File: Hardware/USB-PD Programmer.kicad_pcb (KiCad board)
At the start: 2 copper layers, 34 x 34 mm, 24 parts, among them J1 Conn_01x08_Male, J2 Conn_01x04_Male, J3 Conn_01x02_Male, J4 Conn_01x02_Male, J5 Conn_01x02_Male, J6 Conn_01x02_Male, J7 Conn_01x07_Male, U1 R1501J033B-T1-JE, U2 CH340G, Y1 12M

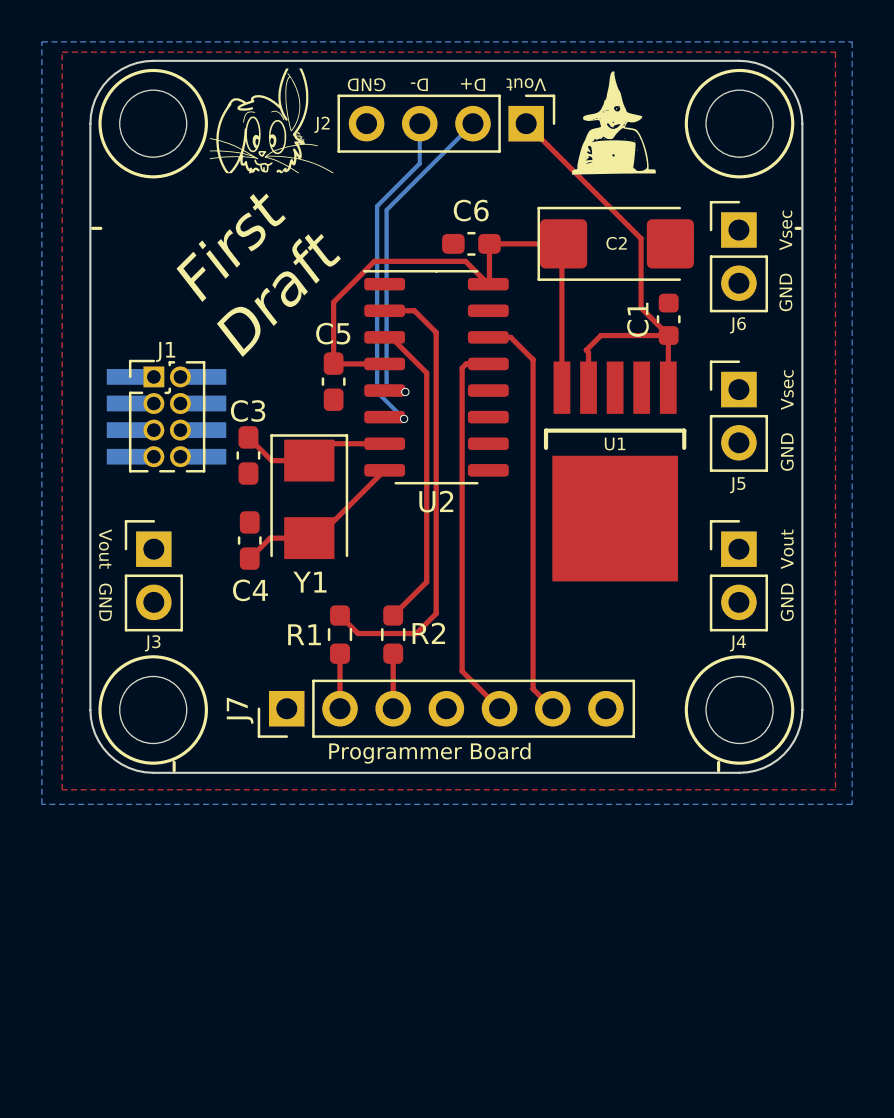
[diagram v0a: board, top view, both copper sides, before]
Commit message: Cleaned up design of the Programmer board
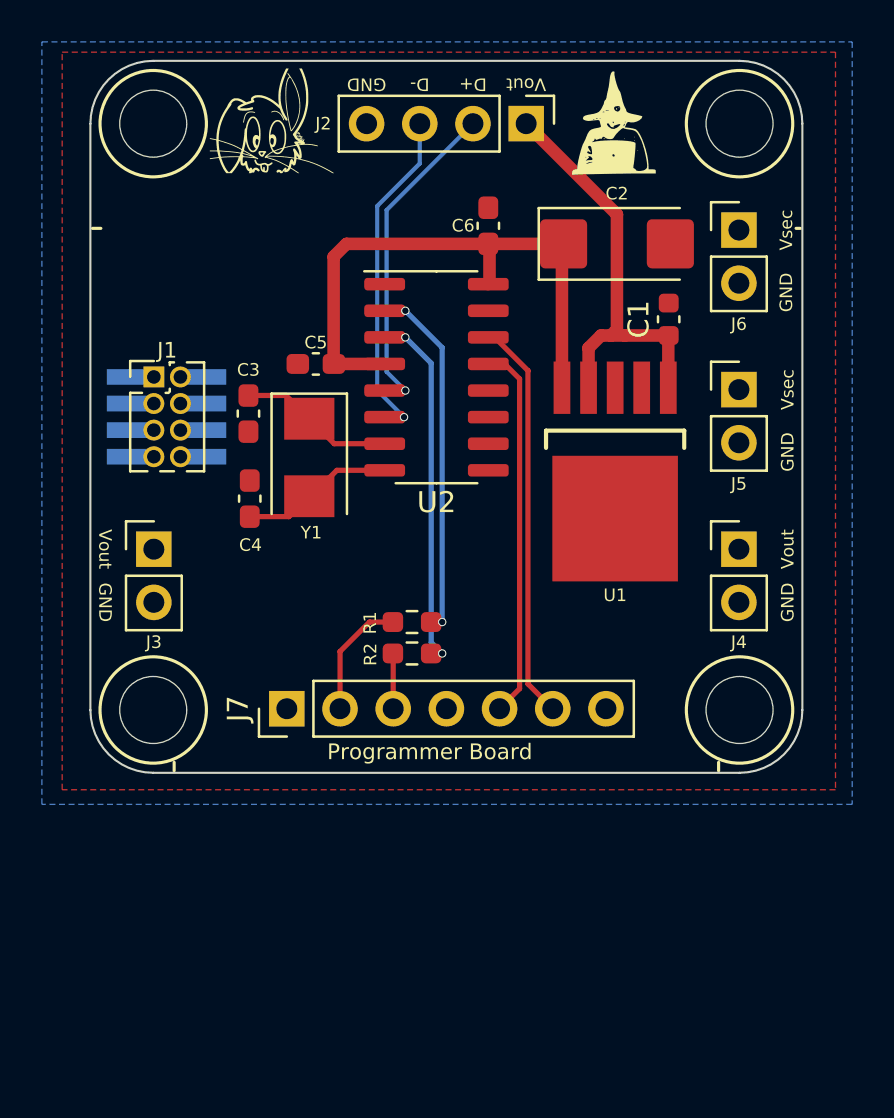
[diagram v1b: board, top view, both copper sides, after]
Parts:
- C3, C4: value 22p -> 20p
- moved R1 3.49 mm to (98.4, 96.8), turned to 180 degrees
- moved C3 2.00 mm to (90.5, 86.8)
- moved C4 2.00 mm to (90.6, 90.9)
- moved Y1 2.00 mm to (93.5, 88.9)
- moved R2 1.27 mm to (98.4, 98.3), turned to 180 degrees
- moved C5 1.20 mm to (93.8, 84.5), turned to 180 degrees
- moved C6 1.18 mm to (102.0, 77.9), turned to 90 degrees
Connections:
- net RxD renamed IO3
- net TxD renamed IO1
- net Vcc2 renamed Vsec
- J7 pad 4: unconnected-(J7-Pad4) -> GND
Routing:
- net Net-(R1-Pad1): track 21.7 -> 15.6 mm, vias 0 -> 2
- net IO3: track 2.53 -> 5.84 mm
- net Vsec: track 26.4 -> 27.6 mm
- net Vout: track 21.5 -> 20.5 mm
- net Net-(R2-Pad1): track 15.0 -> 15.8 mm, vias 0 -> 2
- net /XO: track 8.19 -> 7.36 mm
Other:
- board text removed: "First Draft"

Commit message: Documentation...
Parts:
- added JP1: SolderJumper_2_Open, Tinker:SolderJumper-2_P_Open_Rounded_skinny, F.Cu at (93.3, 78.7)
- U2: value CH340G -> CH340G/C
- moved G*** 17.6 mm to (90.4, 72.9)
- moved REF** 16.6 mm to (108.0, 73.5)
- renumbered J7 to J1, J1 to J7
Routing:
- net +3V3: track 0.00 -> 22.4 mm, vias 0 -> 1
- net Vsec: track 27.6 -> 28.6 mm
- net DTR: track 17.9 -> 17.1 mm, vias 0 -> 1
- net RTS: track 19.2 -> 19.4 mm, vias 0 -> 1
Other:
- board text added: "3v3"
- board text added: "DTR"
- board text added: "RST"
- board text added: "RTS"
- board text added: "RxD"
- board text added: "TxD"

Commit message: Tinkerin' + RESET & LED on Programmer...
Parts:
- added D2: XL-2012RGBC, Tinker:XL-2012RGBC, F.Cu at (96.2, 97.4)
- added R4: 10K, Resistor_SMD:R_0603_1608Metric_Pad0.98x0.95mm_HandSolder, F.Cu at (100.0, 97.4)
- added SW1: SW_Push, Tinker:SW_Push_TS273014TP, F.Cu at (105.8, 96.5)
- moved R1 5.32 mm to (98.4, 91.5)
- moved R2 5.32 mm to (98.4, 93.0)
- moved C1 1.94 mm to (108.9, 81.4), turned to 0 degrees
- moved U1 0.60 mm to (108.1, 89.1)
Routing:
- net +3V3: track 22.4 -> 51.0 mm
- net RST: track 0.00 -> 7.27 mm
- net IO1: track 2.53 -> 8.59 mm
- net Net-(R2-Pad1): track 15.8 -> 10.5 mm
- net Net-(R1-Pad1): track 15.6 -> 10.3 mm
- net IO3: track 5.84 -> 10.6 mm
- net Net-(D2-Pad3): track 0.00 -> 2.86 mm
- net GND: track 0.00 -> 2.63 mm, vias 0 -> 9
- net Vout: track 20.5 -> 19.3 mm
- net Vsec: track 28.6 -> 28.0 mm
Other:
- board text added: "${TITLE}"
- board text added: "NerdMage Modules ${TITLE} (v${REVISION})"
- board text added: "R - TxD G - Rxd"
- board text added: "RESET"
- board text removed: "NerdMage Modules (v0.0.1)"
- board text removed: "Programmer Board"

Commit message: Programmer Board Indicators!
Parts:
- removed D2: XL-2012RGBC, Tinker:XL-2012RGBC
- removed R4: 10K, Resistor_SMD:R_0603_1608Metric_Pad0.98x0.95mm_HandSolder
- added D4: red, LED_SMD:LED_0603_1608Metric, F.Cu at (97.5, 97.6)
- added D5: green, LED_SMD:LED_0603_1608Metric, F.Cu at (94.9, 97.6)
- added D6: yellow, LED_SMD:LED_0603_1608Metric, F.Cu at (102.5, 97.6)
- added D7: yellow, LED_SMD:LED_0603_1608Metric, F.Cu at (105.1, 97.6)
- added R6: 1k, Resistor_SMD:R_0603_1608Metric, F.Cu at (97.5, 94.6)
- added R7: 1k, Resistor_SMD:R_0603_1608Metric, F.Cu at (94.9, 94.6)
- added R8: 1k, Resistor_SMD:R_0603_1608Metric, F.Cu at (102.5, 94.6)
- added R9: 1k, Resistor_SMD:R_0603_1608Metric, F.Cu at (105.1, 94.6)
- moved SW1 14.4 mm to (91.4, 95.8), turned to 90 degrees
- moved C4 1.90 mm to (91.2, 89.1)
- moved R1 1.80 mm to (98.4, 89.7)
- moved R2 1.80 mm to (98.4, 91.2)
- moved Y1 1.55 mm to (93.9, 87.4)
- moved C5 1.54 mm to (94.1, 83.0)
- moved C1 1.50 mm to (108.9, 79.9)
- moved C2 1.50 mm to (108.1, 77.2)
- moved C6 1.50 mm to (102.0, 76.4)
- moved U1 1.50 mm to (108.1, 87.6)
- moved U2 1.50 mm to (99.5, 83.6)
- moved C3 1.32 mm to (91.2, 85.7)
- moved JP1 1.12 mm to (93.6, 79.8)
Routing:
- net +3V3: track 51.0 -> 28.2 mm
- net RST: track 7.27 -> 25.9 mm
- net Vsec: track 28.0 -> 40.3 mm
- net DTR: track 17.1 -> 21.1 mm
- net RTS: track 19.4 -> 23.5 mm
- net Net-(D2-Pad3): track 2.86 -> 0.00 mm
- net GND: track 2.63 -> 0.00 mm
- net IO3: track 10.6 -> 12.7 mm
- net IO1: track 8.59 -> 10.4 mm
- net UD-: track 15.4 -> 13.9 mm
- net UD+: track 14.8 -> 13.3 mm
- net Net-(R8-Pad1): track 0.00 -> 1.39 mm
- net Net-(R7-Pad2): track 0.00 -> 1.39 mm
- net Net-(R6-Pad2): track 0.00 -> 1.39 mm
- net Net-(D7-Pad2): track 0.00 -> 1.39 mm
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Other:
- board text removed: "R - TxD G - Rxd"

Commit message: possibly, maybe, finalised Programmer Board?
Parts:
- moved SW1 17.9 mm to (109.3, 96.2), turned to -90 degrees
- moved R2 0.60 mm to (98.4, 91.8)
- moved U1 0.50 mm to (108.1, 87.1)
- moved R1 0.30 mm to (98.4, 90.0)
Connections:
- SW1 pad 2: +3V3 -> Vsec
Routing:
- net RST: track 25.9 -> 7.64 mm
- net +3V3: track 28.2 -> 21.2 mm
- net Vsec: track 40.3 -> 47.3 mm
- net Vout: track 19.0 -> 18.1 mm
- net Net-(R2-Pad1): track 10.2 -> 10.8 mm
- net IO1: track 10.4 -> 9.78 mm
- net GND: vias 9 -> 0

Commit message: Rabbit OCD attack...
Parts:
- added D1: blue, LED_SMD:LED_0603_1608Metric, F.Cu at (92.4, 97.6)
- added R1: 1k, Resistor_SMD:R_0603_1608Metric, F.Cu at (92.4, 94.6)
- renumbered D4 to D2, D5 to D3, D6 to D4, D7 to D5, R6 to R2, R7 to R3, R8 to R4, R9 to R5, R1 to R6, R2 to R7
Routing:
- net +3V3: track 21.2 -> 23.7 mm
- net Net-(D1-Pad1): track 0.00 -> 1.39 mm
- net DTR: track 21.1 -> 22.0 mm

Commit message: Uber Rework!
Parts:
- J1: footprint Connector_PinHeader_2.54mm:PinHeader_1x07_P2.54mm_Vertical -> Tinker:Board_Stacker_7
- J2: footprint Tinker:PinHeader_1x04_P2.54mm_Vertical -> Tinker:Board_Stacker_4
- J3, J4, J5, J6: footprint Tinker:PinHeader_1x02_P2.54mm_Vertical -> Tinker:Board_Stacker_2
- moved J1 13.6 mm to (96.2, 114.0)
- moved C6 13.3 mm to (102.0, 89.7)
- moved G*** 13.3 mm to (93.0, 85.9)
- moved SW1 13.2 mm to (107.8, 109.3), turned to 180 degrees
- moved J2 13.1 mm to (101.9, 86.0)
- moved D1 13.0 mm to (94.9, 110.4)
- moved R1 13.0 mm to (94.9, 107.4)
- moved REF** 13.0 mm to (107.0, 86.5)
- moved J3 13.0 mm to (86.0, 106.3)
- moved J5 13.0 mm to (114.0, 98.7)
- moved J6 13.0 mm to (114.0, 91.1)
- moved J7 13.0 mm to (86.0, 98.1)
- moved C1 13.0 mm to (108.9, 92.9)
- moved C2 13.0 mm to (108.1, 90.2)
- moved C3 13.0 mm to (91.2, 98.7)
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- renumbered D3 to D2, D2 to D3, R3 to R2, R2 to R3
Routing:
- net +3V3: track 23.7 -> 26.2 mm
- net Vout: track 18.1 -> 20.0 mm
- net DTR: track 22.0 -> 20.8 mm
- net Vsec: track 47.3 -> 46.4 mm
- net RST: track 7.64 -> 8.44 mm
- net RTS: track 23.5 -> 22.7 mm
- net GND: vias 0 -> 1

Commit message: Buncha cosmetic stuff...
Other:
- board text added: "Stacked Rabbit ${TITLE} (v${REVISION})"
- board text removed: "NerdMage Modules ${TITLE} (v${REVISION})"
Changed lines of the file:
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@@
   (gr_line (start 86 117) (end 114 117) (layer "Edge.Cuts") (width 0.1))
   (gr_arc (start 117 114) (mid 116.12132 116.12132) (end 114 117) (layer "Edge.Cuts") (width 0.1))
-  (gr_text "NerdMage Modules\n${TITLE} (v${REVISION})" (at 100 90) (layer "B.SilkS")
+  (gr_text "Stacked Rabbit\n${TITLE} (v${REVISION})" (at 100 90) (layer "B.SilkS")
     (effects (font (size 1 1) (thickness 0.15)) (justify mirror))
   )
